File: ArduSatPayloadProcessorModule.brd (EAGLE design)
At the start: 95.5 x 90.3 mm, 316 parts, among them IC1 ATMEGA328P QFN32, IC10 ATMEGA328P QFN32, IC11 ATMEGA328P QFN32, IC12 ATMEGA328P QFN32, IC13 ATMEGA328P QFN32, IC14 ATMEGA328P QFN32, IC15 ATMEGA328P QFN32, IC16 ATMEGA328P QFN32, IC18 TMP102, IC19 TMP102, IC2 ATMEGA328P QFN32, IC20 ATMEGA2561-16MU, IC3 ATMEGA328P QFN32, IC4 ATMEGA328P QFN32, IC5 ATMEGA328P QFN32, IC6 ATMEGA328P QFN32, IC7 ATMEGA328P QFN32, IC8 ATMEGA328P QFN32, IC9 ATMEGA328P QFN32, P14 microSD, P5 S_ICSP, Q1 RJU003N03 N-MOSFET, Q10 RJU003N03 N-MOSFET, Q11 RJU003N03 N-MOSFET, Q12 RJU003N03 N-MOSFET, Q13 RJU003N03 N-MOSFET, Q14 RJU003N03 N-MOSFET, Q15 RJU003N03 N-MOSFET, Q16 RJU003N03 N-MOSFET, Q17 RJU003N03 N-MOSFET, Q18 RJU003N03 N-MOSFET, Q19 RJU003N03 N-MOSFET, Q2 RJU003N03 N-MOSFET, Q20 RJU003N03 N-MOSFET, Q21 RJU003N03 N-MOSFET, Q22 RJU003N03 N-MOSFET, Q23 RJU003N03 N-MOSFET, Q24 RJU003N03 N-MOSFET, Q25 RJU003N03 N-MOSFET, Q26 RJU003N03 N-MOSFET, Q27 RJU003N03 N-MOSFET, Q28 RJU003N03 N-MOSFET, Q29 RJU003N03 N-MOSFET, Q3 RJU003N03 N-MOSFET, Q30 RJU003N03 N-MOSFET, Q31 RJU003N03 N-MOSFET, Q32 RJU003N03 N-MOSFET, Q33 RJU003N03 N-MOSFET, Q34 RJU003N03 N-MOSFET, Q35 RJU003N03 N-MOSFET, Q36 RJU003N03 N-MOSFET, Q39 RJU003N03 N-MOSFET, Q4 RJU003N03 N-MOSFET, Q40 RJU003N03 N-MOSFET, Q41 RJU003N03 N-MOSFET, Q42 RJU003N03 N-MOSFET, Q5 RJU003N03 N-MOSFET, Q6 RJU003N03 N-MOSFET, Q7 RJU003N03 N-MOSFET, Q8 RJU003N03 N-MOSFET, Q9 RJU003N03 N-MOSFET, SW1 ADG801SOT23-6, SW10 ADG801SOT23-6, SW11 ADG801SOT23-6, SW12 ADG801SOT23-6, SW13 ADG801SOT23-6, SW14 ADG801SOT23-6, SW15 ADG801SOT23-6, SW16 ADG801SOT23-6, SW2 ADG801SOT23-6, SW3 ADG801SOT23-6, SW4 ADG801SOT23-6, SW5 ADG801SOT23-6, SW6 ADG801SOT23-6, SW7 ADG801SOT23-6, SW8 ADG801SOT23-6, SW9 ADG801SOT23-6, X1 geiger, X2 gps, X4 spectruino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

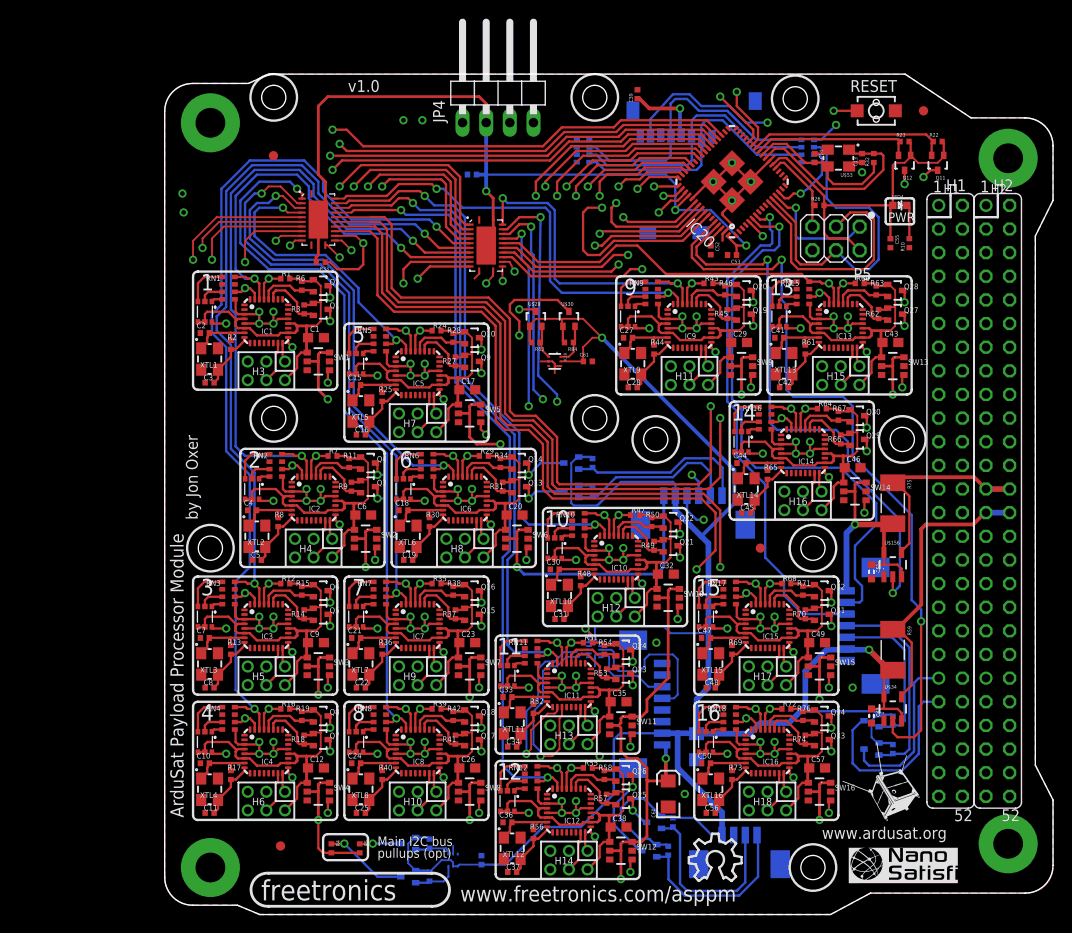
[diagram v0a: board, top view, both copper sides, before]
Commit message: ERC and DRC for production
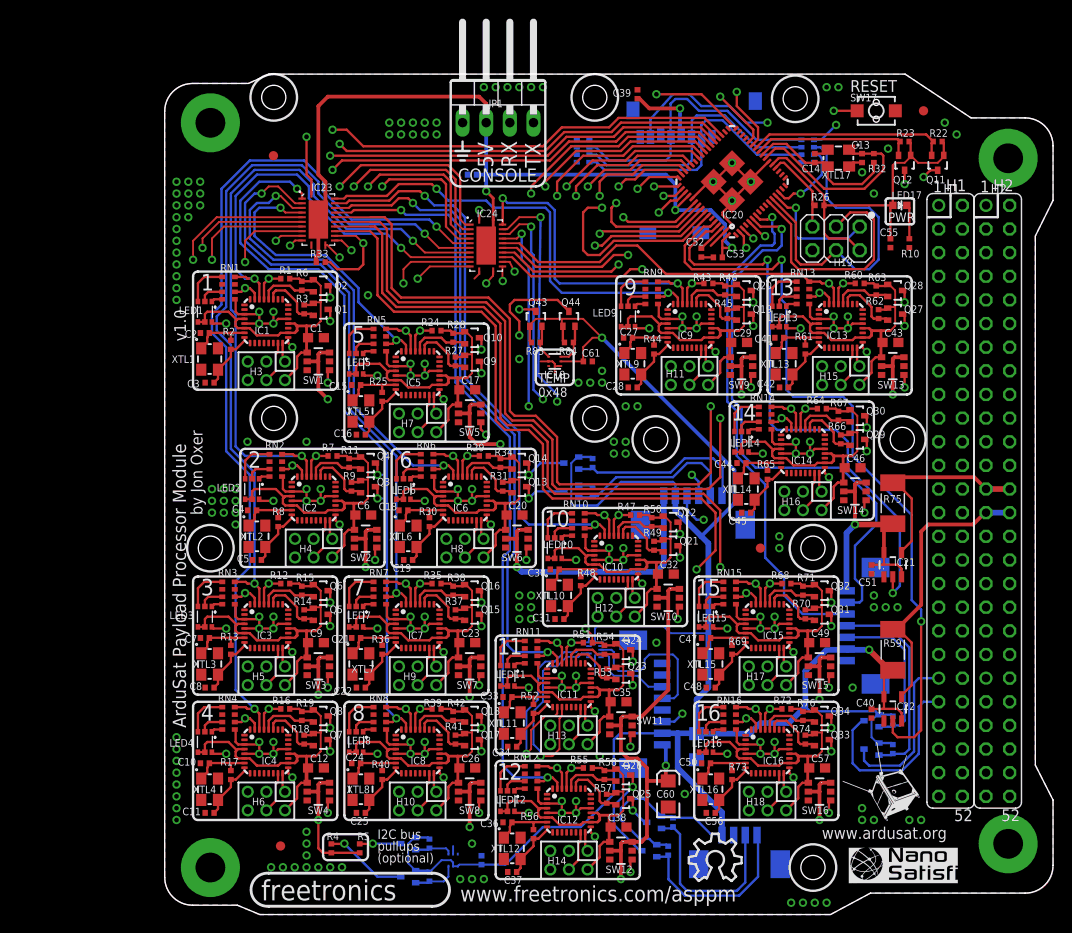
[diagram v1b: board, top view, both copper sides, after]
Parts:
- removed X6: 53398-04, con-molex:53398-04
- added X3: Spectruino, con-molex:53398-07
- C40, C51: device freetronics-master-v1.1:0603 -> freetronics-jon:0402C
- IC21, IC22: value MAX4372 -> MAX4372F
- JP1: value (none) -> DEBUG
- LED17: value RGBLEDSMT -> BLUE 0603; device freetronics-jon:19-337 -> freetronics:LED-0603
- LED4: value PWR/BLUE -> RGBLEDSMT; device freetronics:LED-0603 -> freetronics-jon:19-337
- Q43, Q44, Q45, Q46: value MOSFET-NSOT-323 -> RJU003N03 N-MOSFET
- R59, R75: value 0.15R 2010 -> 0.1R 2010
- RN13: device freetronics-master-v1:CAY16 -> resistor-dil:CAY16
- RN14: value 1K -> 2K2; device freetronics-master-v1:CAY16 -> resistor-dil:CAY16
- RN17: device resistor-dil:CAY16 -> freetronics-master-v1:CAY16
- RN18: value 2K2 -> 1K; device resistor-dil:CAY16 -> freetronics-master-v1:CAY16
- SW1, SW10, SW11, SW12, SW13, SW14, SW15, SW16, SW2, SW3, SW4, SW5, SW6, SW7, SW8, SW9: value ADG801SOT23-6 -> ADG801 SOT23-6
- X1: value geiger -> Geiger
- X4: value spectruino -> Bottom Plate; device con-molex:53398-07 -> con-molex:53398-04
- XTL17: value CRYSTAL-GND3X2 -> SMD3225-16MHZ 3.2 x 2.5mm crystal
- moved LED4 94.3 mm to (4.32, 18.5)
- moved RN18 61.5 mm to (69.1, 82.0), flipped to the bottom
- moved LED17 61.3 mm to (79.0, 76.2)
- moved LED13 59.7 mm to (66.0, 64.3)
- moved LED9 54.3 mm to (49.8, 64.3)
- moved RN17 50.0 mm to (45.0, 82.0), flipped to the bottom
- moved LED5 43.8 mm to (20.6, 59.2)
- moved RN15 33.2 mm to (60.7, 34.5)
- moved RN16 32.5 mm to (60.7, 21.1)
- moved RN14 29.1 mm to (64.5, 53.3), flipped to the top
- moved X4 28.7 mm to (61.8, 6.04), turned to 180 degrees
- moved RN13 28.1 mm to (68.6, 66.8), flipped to the top
- moved LED10 26.1 mm to (41.9, 39.4)
- moved LED15 19.2 mm to (58.2, 32.0)
- moved LED7 14.6 mm to (20.6, 32.0)
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- renumbered JP4 to JP1, P14 to P1, P5 to H19, S1 to SW17, U$156 to IC21, U$26 to IC17, U$29 to Q43, U$30 to Q44, U$31 to Q45, U$32 to Q46, U$34 to IC22, U$53 to XTL17, U$59 to IC24, U$60 to IC23
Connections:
- removed net RX: IC24.1
- removed net S_D38: IC20.32
- removed net TX: IC23.1
- net 3.3V: now also X3.6, X4.4; no longer X4.6, X6.4
- net 5V: now also LED17.A, X3.1; no longer LED4.A, X4.1
- net BOTTOM_SCL: now also X4.1; no longer X6.1
- net BOTTOM_SDA: now also X4.2; no longer X6.2
- net D0_RX: now also IC24.1
- net D1_TX: now also IC23.1
- net GND: now also RN14.1, RN17.2, RN17.3, X3.7, X4.3; no longer RN13.2, RN13.3, RN18.1, X4.7, X6.3
- net N$14: now also LED17.C; no longer LED4.C
- net N$23: now also RN17.8, RN18.2; no longer RN13.8, RN14.2
- net N$2356: now also LED4.2; no longer LED5.2
- net N$2357: now also LED4.1; no longer LED5.1
- net N$2358: now also LED4.3; no longer LED5.3
- net N$2944: now also LED5.2; no longer LED6.2
- net N$2945: now also LED5.1; no longer LED6.1
- net N$2946: now also LED5.3; no longer LED6.3
- net N$321: now also RN17.6, RN18.4; no longer RN13.6, RN14.4
- net N$3532: now also LED6.2; no longer LED7.2
- net N$3533: now also LED6.1; no longer LED7.1
- net N$3534: now also LED6.3; no longer LED7.3
- net N$4120: now also LED7.2; no longer LED8.2
- net N$4121: now also LED7.1; no longer LED8.1
- net N$4122: now also LED7.3; no longer LED8.3
- net N$4708: now also LED8.2; no longer LED9.2
- net N$4709: now also LED8.1; no longer LED9.1
- net N$4710: now also LED8.3; no longer LED9.3
- net N$5296: now also LED9.2; no longer LED10.2
- net N$5297: now also LED9.1; no longer LED10.1
- net N$5298: now also LED9.3; no longer LED10.3
- net N$5884: now also LED10.2; no longer LED11.2
- net N$5885: now also LED10.1; no longer LED11.1
- net N$5886: now also LED10.3; no longer LED11.3
- net N$6472: now also LED11.2; no longer LED12.2
- net N$6473: now also LED11.1; no longer LED12.1
- net N$6474: now also LED11.3; no longer LED12.3
- net N$7060: now also LED12.2; no longer LED13.2
- net N$7061: now also LED12.1; no longer LED13.1
- net N$7062: now also LED12.3; no longer LED13.3
- net N$7648: now also LED13.2, RN13.7; no longer LED14.2, RN15.7
- net N$7649: now also LED13.1, RN13.8; no longer LED14.1, RN15.8
- net N$7650: now also LED13.3, RN13.5; no longer LED14.3, RN15.5
- net N$8236: now also LED14.2, RN14.7; no longer LED15.2, RN16.7
- net N$8237: now also LED14.1, RN14.8; no longer LED15.1, RN16.8
- net N$8238: now also LED14.3, RN14.5; no longer LED15.3, RN16.5
- net N$8824: now also LED15.2, RN15.7; no longer LED16.2, RN17.7
- net N$8825: now also LED15.1, RN15.8; no longer LED16.1, RN17.8
- net N$8826: now also LED15.3, RN15.5; no longer LED16.3, RN17.5
- net N$90: now also RN17.7, RN18.3; no longer RN13.7, RN14.3
- net N$9412: now also LED16.2, RN16.7; no longer LED17.2, RN18.7
- net N$9413: now also LED16.1, RN16.8; no longer LED17.1, RN18.8
- net N$9414: now also LED16.3, RN16.5; no longer LED17.3, RN18.5
- net N10_5V: now also LED10.5, LED10.6; no longer LED11.5, LED11.6
- net N10_D13_SCK: now also LED10.4; no longer LED11.4
- net N11_5V: now also LED11.5, LED11.6; no longer LED12.5, LED12.6
- net N11_D13_SCK: now also LED11.4; no longer LED12.4
- net N12_5V: now also LED12.5, LED12.6; no longer LED13.5, LED13.6
- net N12_D13_SCK: now also LED12.4; no longer LED13.4
- net N13_5V: now also LED13.5, LED13.6; no longer LED14.5, LED14.6
- net N13_D0_RX: now also RN13.4; no longer RN15.4
- net N13_D13_SCK: now also LED13.4; no longer LED14.4
- net N13_D1_TX: now also RN13.2; no longer RN15.2
- net N14_5V: now also LED14.5, LED14.6; no longer LED15.5, LED15.6
- net N14_D0_RX: now also RN14.4; no longer RN16.4
- net N14_D13_SCK: now also LED14.4; no longer LED15.4
- net N14_D1_TX: now also RN14.2; no longer RN16.2
- net N15_5V: now also LED15.5, LED15.6; no longer LED16.5, LED16.6
- net N15_D0_RX: now also RN15.4; no longer RN17.4
- net N15_D13_SCK: now also LED15.4; no longer LED16.4
- net N15_D1_TX: now also RN15.2; no longer RN17.2
- net N16_5V: now also LED16.5, LED16.6; no longer LED17.5, LED17.6
- net N16_D0_RX: now also RN16.4; no longer RN18.4
- net N16_D13_SCK: now also LED16.4; no longer LED17.4
- net N16_D1_TX: now also RN16.2; no longer RN18.2
- net N4_5V: now also LED4.5, LED4.6; no longer LED5.5, LED5.6
- net N4_D13_SCK: now also LED4.4; no longer LED5.4
- net N5_5V: now also LED5.5, LED5.6; no longer LED6.5, LED6.6
- net N5_D13_SCK: now also LED5.4; no longer LED6.4
- net N6_5V: now also LED6.5, LED6.6; no longer LED7.5, LED7.6
- net N6_D13_SCK: now also LED6.4; no longer LED7.4
- net N7_5V: now also LED7.5, LED7.6; no longer LED8.5, LED8.6
- net N7_D13_SCK: now also LED7.4; no longer LED8.4
- net N8_5V: now also LED8.5, LED8.6; no longer LED9.5, LED9.6
- net N8_D13_SCK: now also LED8.4; no longer LED9.4
- net N9_5V: now also LED9.5, LED9.6; no longer LED10.5, LED10.6
- net N9_D13_SCK: now also LED9.4; no longer LED10.4
- net PWR_SPEC: now also X3.2; no longer X4.2
- net RST_GPS: now also IC20.32
- net RST_SPEC: now also X3.3; no longer X4.3
- net SPEC_SCL: now also X3.5; no longer X4.5
- net SPEC_SDA: now also X3.4; no longer X4.4
- net S_D10: now also RN18.7; no longer RN14.7
- net S_D51_MOSI: now also RN18.6; no longer RN14.6
- net S_D52_SCK: now also RN18.5; no longer RN14.5
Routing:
- net RST_GPS: track 0.00 -> 115.3 mm, vias 0 -> 2
- net D1_TX: track 0.00 -> 63.3 mm, vias 0 -> 2
- net D0_RX: track 0.00 -> 40.5 mm, vias 0 -> 2
- net N11_D0_RX: track 62.4 -> 54.1 mm
- net 5V: track 600.1 -> 604.9 mm
- net N12_D0_RX: track 74.6 -> 72.4 mm
- net S_A1: track 80.2 -> 81.9 mm
- net S_A0: track 59.9 -> 61.7 mm
- net GND: track 221.6 -> 223.1 mm, vias 78 -> 181
- net D23_N14_PWR: track 56.2 -> 55.3 mm
- net N$22: track 2.37 -> 3.06 mm
- net D33_N8_PWR: track 99.4 -> 100.0 mm
- net N15_D0_RX: track 64.9 -> 64.3 mm
- net N14_D0_RX: track 51.4 -> 50.8 mm
- net N16_D0_RX: track 77.2 -> 76.7 mm
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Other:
- board text added: "(optional)"
- board text added: "0x48"
- board text added: "0x49"
- board text added: "5V"
- board text added: "CONSOLE"
- board text added: "Copyright 2013 Freetronics Pty Ltd www.freetronics.com/asppm Released under the TAPR Open Hardware Licence www.tapr.org/OHL SKU: ASPPM"
- board text added: "I2C bus"
- board text added: "IC17"
- board text added: "IC23"
- board text added: "IC24"
- board text added: "LED1"
- board text added: "LED10"
- board text added: "LED11"
- board text added: "LED12"
- board text added: "LED13"
- board text added: "LED14"
- board text added: "LED15"
- board text added: "LED16"
- board text added: "LED2"
- board text added: "LED3"
- board text added: "LED4"
- board text added: "LED5"
- board text added: "LED6"
- board text added: "LED7"
- board text added: "LED8"
- board text added: "LED9"
- board text added: "RX"
- board text added: "SW17"
- board text added: "TEMP"
- board text added: "TX"
- board text added: "pullups"
- board text removed: "(c) 2013 Freetronics Pty Ltd"
- board text removed: "Main I2C bus"
- board text removed: "pullups (opt)"

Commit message: Fix footprint for RGB LED
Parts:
- LED1, LED10, LED11, LED12, LED13, LED14, LED15, LED16, LED2, LED3, LED4, LED5, LED6, LED7, LED8, LED9: value RGBLEDSMT -> FREETRONICS-MASTER-V1_RGBLEDSMT; device freetronics-jon:19-337 -> freetronics-master-v1:FREETRONICS-MASTER-V1_19-337
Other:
- board text added: "v1.1"
- board text removed: "v1.0"

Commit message: Fixed ISP pin assignment Added D13 LED to supervisor Fixed TX/RX from supervisor to multiplexers Replaced 4-pin debug connector with 6-pin connector in FTDI-type format Linked supervisor reset to debug connector GPS power now controlled by supervisor Input power from debug connector now goes through 5V current sensor Switched Cubesat Bus power links to H1-51 (5V) and H1-52 (3.3V) Added cut-track jumpers to select power link source Linked debug console to Cubesat Bus H1-34 (TXO) and H1-36 (RXD) Moved debug connector away from edge to increase solar panel clearance
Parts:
- added C58: 100nF 0402, freetronics-jon:0402C
- added LED18: BLUE 0603, freetronics-jon:LED-0402
- added R81: 2K2 0402, freetronics-jon:0402
- added SJ1, SJ2, SJ3, SJ4: (no value), freetronics-master-v1.1:SJ
- added SW18: ADG801 SOT23-6, freetronics-jon:SOT23-6
- C13, C14: value 22pF 0603 -> 22pF 0402
- JP1: device pinhead:1X04/90 -> freetronics-master-v1:MOLEX-1X6-RA
- moved C54 17.2 mm to (17.3, 86.4)
- moved JP1 11.9 mm to (26.7, 81.3)
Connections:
- removed net AREF: C14.2, IC20.24, R32.1, XTL17.3
- removed net H1R34: H1.34
- removed net H1R36: H1.36
- removed net H2L51: H2.51
- removed net H2R52: H2.52
- new net +3V3_AS: H2.52, SJ3.1
- new net +3V3_SRC: IC22.4, R59.1, SJ3.2, SJ4.2
- new net +5V_AS: H2.51, SJ1.1
- new net +5V_SRC: IC21.4, JP1.3, R75.1, SJ1.2, SJ2.2
- new net GPS_5V: C60.A, SW18.1, X2.1
- new net N$9998: LED18.C, R81.2
- new net PWR_GPS: IC20.31, SW18.4
- new net RTS: C58.1, JP1.6
- new net XTAL2: C13.2, IC20.23, R32.2, XTL17.1
- net +5V_SYS: now also SJ2.1; no longer IC21.4, R75.1
- net 5V: now also SW18.2, SW18.6; no longer C60.A, JP1.2, X2.1
- net D0_RX: now also H19.4, IC23.1; no longer IC24.1
- net D1_TX: now also H19.1, IC24.1; no longer IC23.1
- net GND: now also JP1.2, R81.1, SW18.3
- net RXD1: now also H1.36, JP1.4; no longer JP1.3
- net S_D13: now also LED18.A
- net S_D50_MISO: no longer H19.1
- net S_D51_MOSI: no longer H19.4
- net S_RESET: now also C58.2
- net TXD1: now also H1.34, JP1.5; no longer JP1.4
- net VCC_SYS: now also SJ4.1; no longer IC22.4, R59.1
- net XTAL1: now also C14.2, IC20.24, R32.1, XTL17.3; no longer C13.2, IC20.23, R32.2, XTL17.1
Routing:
- net +5V_SRC: track 0.00 -> 230.2 mm, vias 0 -> 2
- net PWR_GPS: track 0.00 -> 126.7 mm, vias 0 -> 2
- net TXD1: track 28.4 -> 108.2 mm, vias 1 -> 2
- net RXD1: track 37.0 -> 116.6 mm, vias 1 -> 2
- net S_RESET: track 25.8 -> 66.2 mm
- net D0_RX: track 40.5 -> 78.9 mm
- net +3V3_SRC: track 0.00 -> 31.6 mm, vias 0 -> 2
- net +5V_SYS: track 22.8 -> 52.9 mm
- net S_D51_MOSI: track 36.1 -> 13.7 mm, vias 0 -> 1
- net XTAL2: track 0.00 -> 21.0 mm
- net AREF: track 16.6 -> 0.00 mm
- net +5V_AS: track 0.00 -> 16.5 mm
- net 5V: track 604.9 -> 589.0 mm
- net VCC_SYS: track 31.2 -> 46.3 mm, vias 0 -> 2
- net S_A1: track 81.9 -> 96.1 mm
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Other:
- board text added: "BLACK"
- board text added: "CTS"
- board text added: "D13"
- board text added: "GREEN"
- board text added: "RTS"

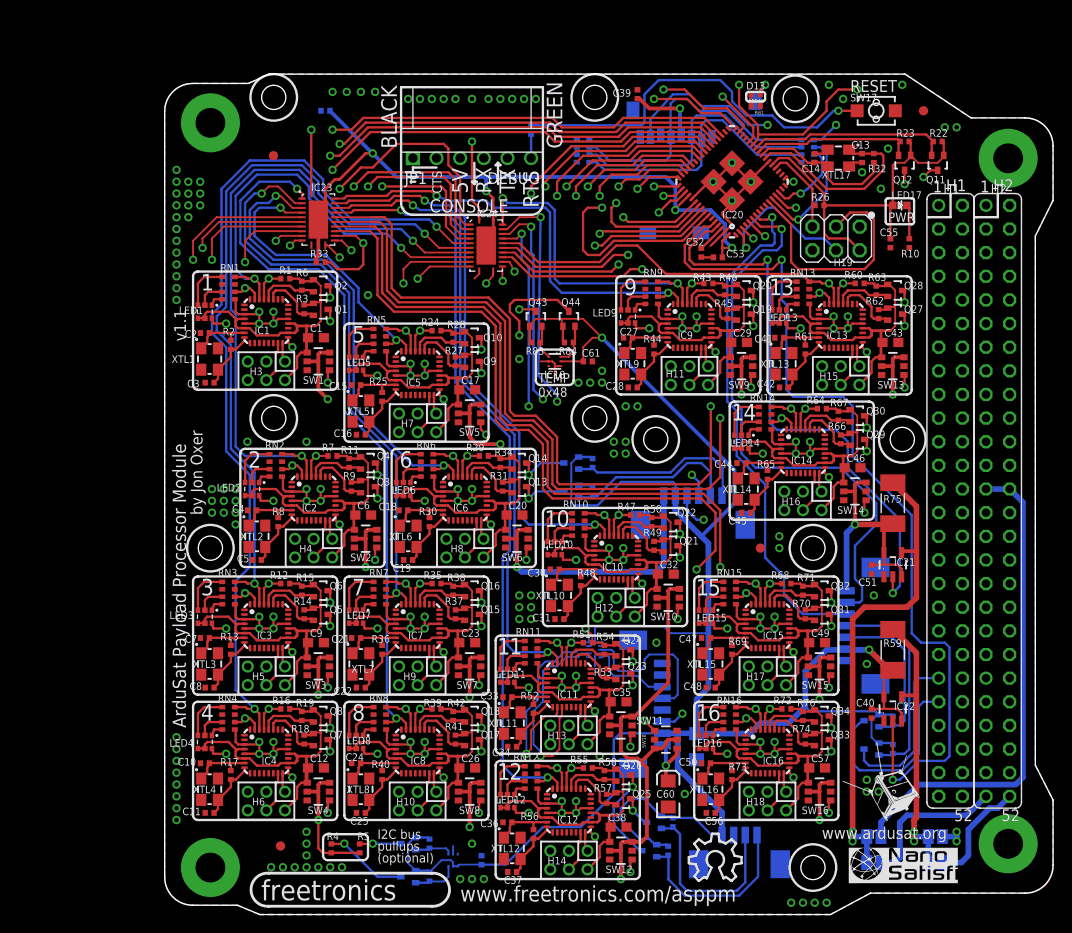
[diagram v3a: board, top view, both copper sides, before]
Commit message: Added labels for power source selection jumpers; added parts for node reset latch
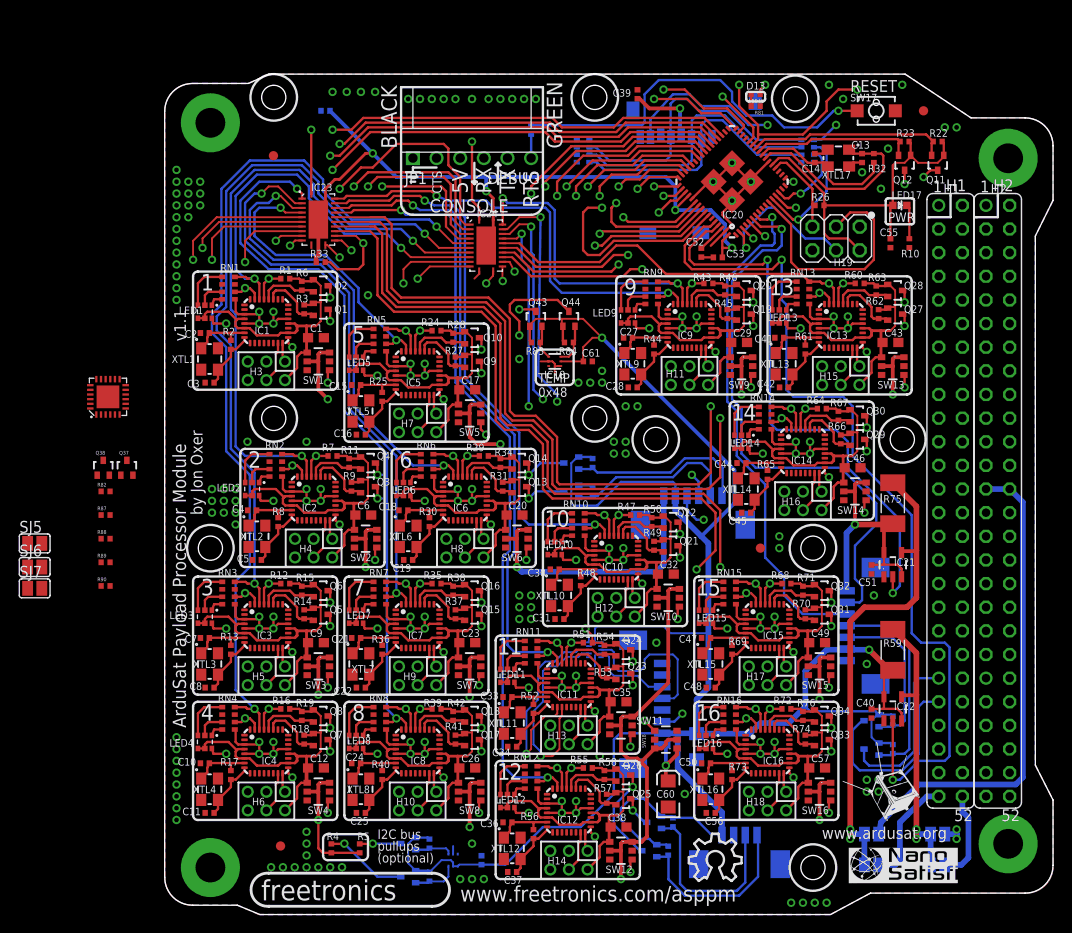
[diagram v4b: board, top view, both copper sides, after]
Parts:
- added Q37, Q38: RJU003N03 N-MOSFET, freetronics-jon:SOT32-3
- added R82, R87: 4K7 0402, freetronics-jon:0402
- added R88, R89, R90: 10K 0402, freetronics-jon:0402
- added SJ5, SJ6, SJ7: (no value), freetronics-master-v1:SJ
- added U$26: TCA9555QFN, freetronics-jon:QFN-24
- moved SJ1 0.36 mm to (75.9, 5.33)
- moved SJ3 0.36 mm to (83.1, 5.33)
- moved SJ2 0.36 mm to (75.9, 8.64)
- moved SJ4 0.36 mm to (83.1, 8.64)
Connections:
- removed net H1L51: H1.51
- removed net H1R52: H1.52
- new net H2L51: H2.51
- new net H2R52: H2.52
- new net N$10000: R90.2, SJ5.1, U$26.18
- new net N$10004: R89.2, SJ6.1, U$26.23
- new net N$10005: R88.2, SJ7.1, U$26.24
- new net N$10006: Q37.2, R82.1, U$26.19
- new net N$10007: Q38.2, R87.1, U$26.20
- net +3V3_AS: now also H1.52; no longer H2.52
- net +5V_AS: now also H1.51; no longer H2.51
- net 5V: now also Q37.1, Q38.1, R82.2, R87.2, SJ5.2, SJ6.2, SJ7.2, U$26.21
- net GND: now also R88.1, R89.1, R90.1, U$26.9, U$26.TGND
- net N10_RESET: now also U$26.11
- net N11_RESET: now also U$26.12
- net N12_RESET: now also U$26.13
- net N13_RESET: now also U$26.14
- net N14_RESET: now also U$26.15
- net N15_RESET: now also U$26.16
- net N16_RESET: now also U$26.17
- net N1_RESET: now also U$26.1
- net N2_RESET: now also U$26.2
- net N3_RESET: now also U$26.3
- net N4_RESET: now also U$26.4
- net N5_RESET: now also U$26.5
- net N6_RESET: now also U$26.6
- net N7_RESET: now also U$26.7
- net N8_RESET: now also U$26.8
- net N9_RESET: now also U$26.10
- net SCL: now also Q37.3
- net SDA: now also Q38.3
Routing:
- net +5V_AS: track 16.5 -> 11.9 mm
- net +3V3_AS: track 11.8 -> 9.73 mm
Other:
- board text added: "3V3"
- board text added: "BUS POWER"
- board text added: "H1:51"
- board text added: "H1:52"
- board text added: "H2:25/26"
- board text added: "H2:27/28"
